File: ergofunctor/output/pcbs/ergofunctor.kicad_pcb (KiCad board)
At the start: 2 copper layers, 155.9 x 135.1 mm, 50 parts

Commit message: joystick adjustments for ergofunctor
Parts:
- removed TRRS1: TRRS-PJ-320A-dual, TRRS-PJ-320A-dual
- added H1: , ceoloide:mounting_hole_plated, F.Cu at (184.3, 144.1)
- added H2: , ceoloide:mounting_hole_plated, F.Cu at (162.6, 136.2)
- added XX1: , AMPHENOL_SFV5R-4STE1HLF, F.Cu at (179.9, 122.3)
- moved _2 10.0 mm to (173.9, 86.9)
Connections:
- _2 pad 1: pos -> B-
- _2 pad 2: B- -> pos
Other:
- board size 155.9 x 135.1 mm -> 161.5 x 130.8 mm

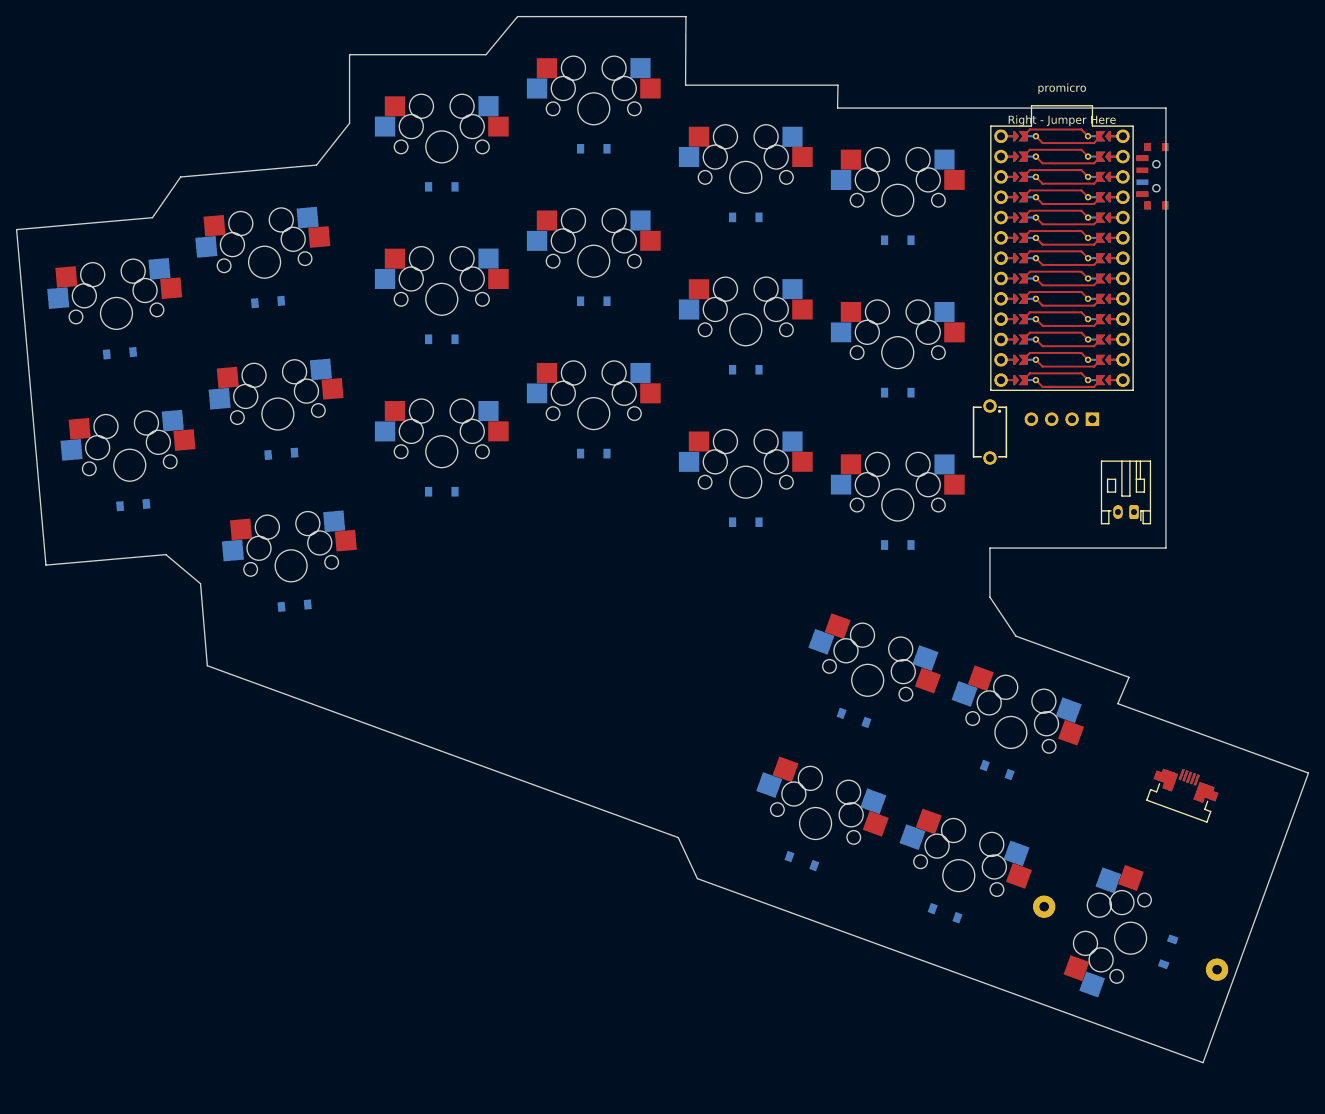
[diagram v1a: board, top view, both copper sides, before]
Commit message: change joystick and finish config
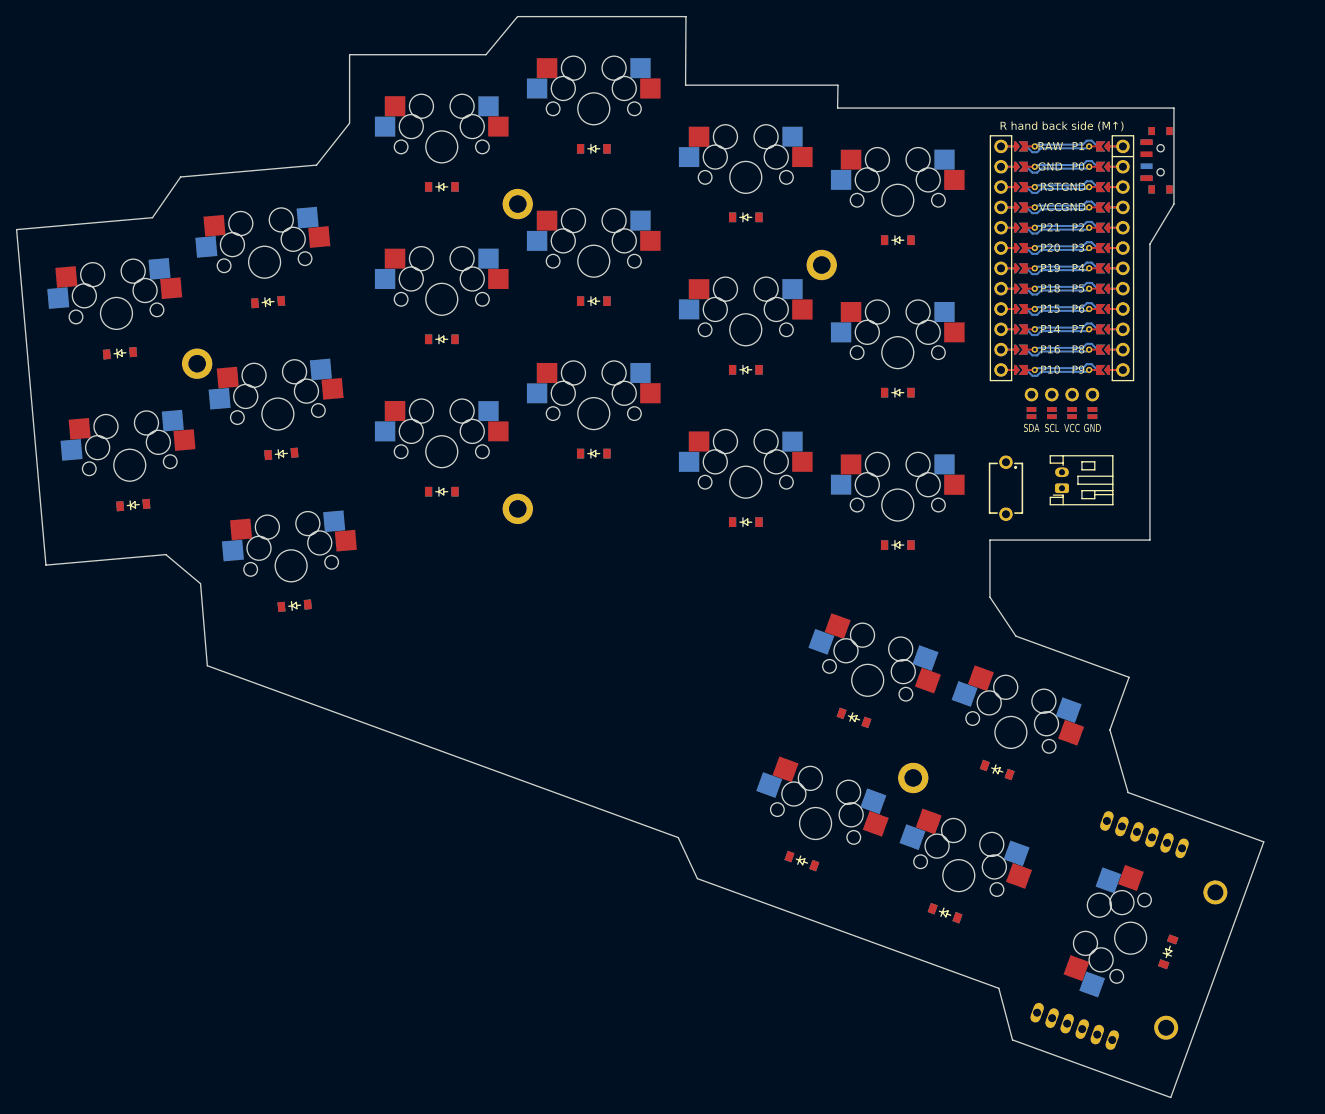
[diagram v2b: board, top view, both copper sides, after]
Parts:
- removed ?: , ProMicro
- removed OLED1: OLED, lib:OLED_headers
- removed _2: , Connector_JST:JST_PH_S2B-PH-K_1x02_P2.00mm_Horizontal
- added DISP1: , nice!view, F.Cu at (164.9, 88.9)
- added H3: , ceoloide:mounting_hole_plated, F.Cu at (96.8, 48.4)
- added H4: , ceoloide:mounting_hole_plated, F.Cu at (96.8, 86.5)
- added H5: , ceoloide:mounting_hole_plated, F.Cu at (146.3, 120.1)
- added MCU1: , ceoloide:mcu_supermini_nrf52840, F.Cu at (164.9, 53.9)
- added XX2: , joystick, F.Cu at (184.0, 134.4)
- added _1: , Connector_JST:JST_PH_S2B-PH-K_1x02_P2.00mm_Horizontal,  at (164.9, 83.9)
- D1, D10, D11, D12, D13, D14, D15, D16, D17, D18, D19, D2, D20, D21, D22, D3, D4, D5, D6, D7, D8, D9: moved to F.Cu
- XX1: footprint AMPHENOL_SFV5R-4STE1HLF -> joystick
- moved H1 148.3 mm to (56.8, 68.3), turned to 5 degrees
- moved H2 84.9 mm to (134.8, 56.0), turned to 0 degrees
- moved XX1 29.1 mm to (177.9, 151.3), turned to 70 degrees
- moved S23 7.30 mm to (157.9, 83.9)
- moved T1 2.07 mm to (176.9, 42.9)
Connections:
- T1 pad 1: pos -> sw1
- T1 pad 2: B+ -> RAW
- XX1 pad 2: P20 -> GND
- XX1 pad 3: P19 -> P20
- XX1 pad 4: GND -> P19
- XX1 pad 5: P21 -> GND
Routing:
- net (no net): track 371.4 -> 337.7 mm
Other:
- board size 161.5 x 130.8 mm -> 155.9 x 135.1 mm

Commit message: fix mcu-switchs connection
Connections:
- D1 pad 1: R_HOME -> P14
- D10 pad 1: R_HOME -> P14
- D11 pad 1: R_TOP -> P15
- D12 pad 1: R_BOT -> P16
- D13 pad 1: R_HOME -> P14
- D14 pad 1: R_TOP -> P15
- D15 pad 1: R_BOT -> P16
- D16 pad 1: R_HOME -> P14
- D17 pad 1: R_TOP -> P15
- D18 pad 1: R_THUMB -> P10
- D19 pad 1: R_THUMB -> P10
- D2 pad 1: R_TOP -> P15
- D20 pad 1: R_THUMB -> P10
- D21 pad 1: R_THUMB -> P10
- D22 pad 1: R_THUMB -> P10
- D3 pad 1: R_BOT -> P16
- D4 pad 1: R_HOME -> P14
- D5 pad 1: R_TOP -> P15
- D6 pad 1: R_BOT -> P16
- D7 pad 1: R_HOME -> P14
- D8 pad 1: R_TOP -> P15
- D9 pad 1: R_BOT -> P16
- S1 pad 1: C_P_OUTER -> P4
- S10 pad 1: C_M_MIDDLE -> P7
- S11 pad 1: C_M_MIDDLE -> P7
- S12 pad 1: C_M_INDEX -> P8
- S13 pad 1: C_M_INDEX -> P8
- S14 pad 1: C_M_INDEX -> P8
- S15 pad 1: C_M_INNER -> P9
- S16 pad 1: C_M_INNER -> P9
- S17 pad 1: C_M_INNER -> P9
- S18 pad 1: C_P_INNER -> P4
- S19 pad 1: C_M_RING -> P5
- S2 pad 1: C_P_OUTER -> P4
- S20 pad 1: C_M_MIDDLE -> P6
- S21 pad 1: C_M_INDEX -> P7
- S22 pad 1: C_M_INNER -> P8
- S3 pad 1: C_P_INNER -> P5
- S4 pad 1: C_P_INNER -> P5
- S5 pad 1: C_P_INNER -> P5
- S6 pad 1: C_M_RING -> P6
- S7 pad 1: C_M_RING -> P6
- S8 pad 1: C_M_RING -> P6
- S9 pad 1: C_M_MIDDLE -> P7

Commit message: fix connected columns
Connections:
- D18 pad 2: outer_row -> outer_top_row
- D19 pad 2: middle_row -> middle_top_row
- D20 pad 2: outer_row -> outer_bottom_row
- D21 pad 2: middle_row -> middle_bottom_row
- D3 pad 2: inner_bottom -> innerp_bottom
- D4 pad 2: inner_home -> innerp_home
- D5 pad 2: inner_top -> innerp_top
- S18 pad 2: outer_row -> outer_top_row
- S19 pad 2: middle_row -> middle_top_row
- S20 pad 2: outer_row -> outer_bottom_row
- S21 pad 2: middle_row -> middle_bottom_row
- S3 pad 2: inner_bottom -> innerp_bottom
- S4 pad 2: inner_home -> innerp_home
- S5 pad 2: inner_top -> innerp_top

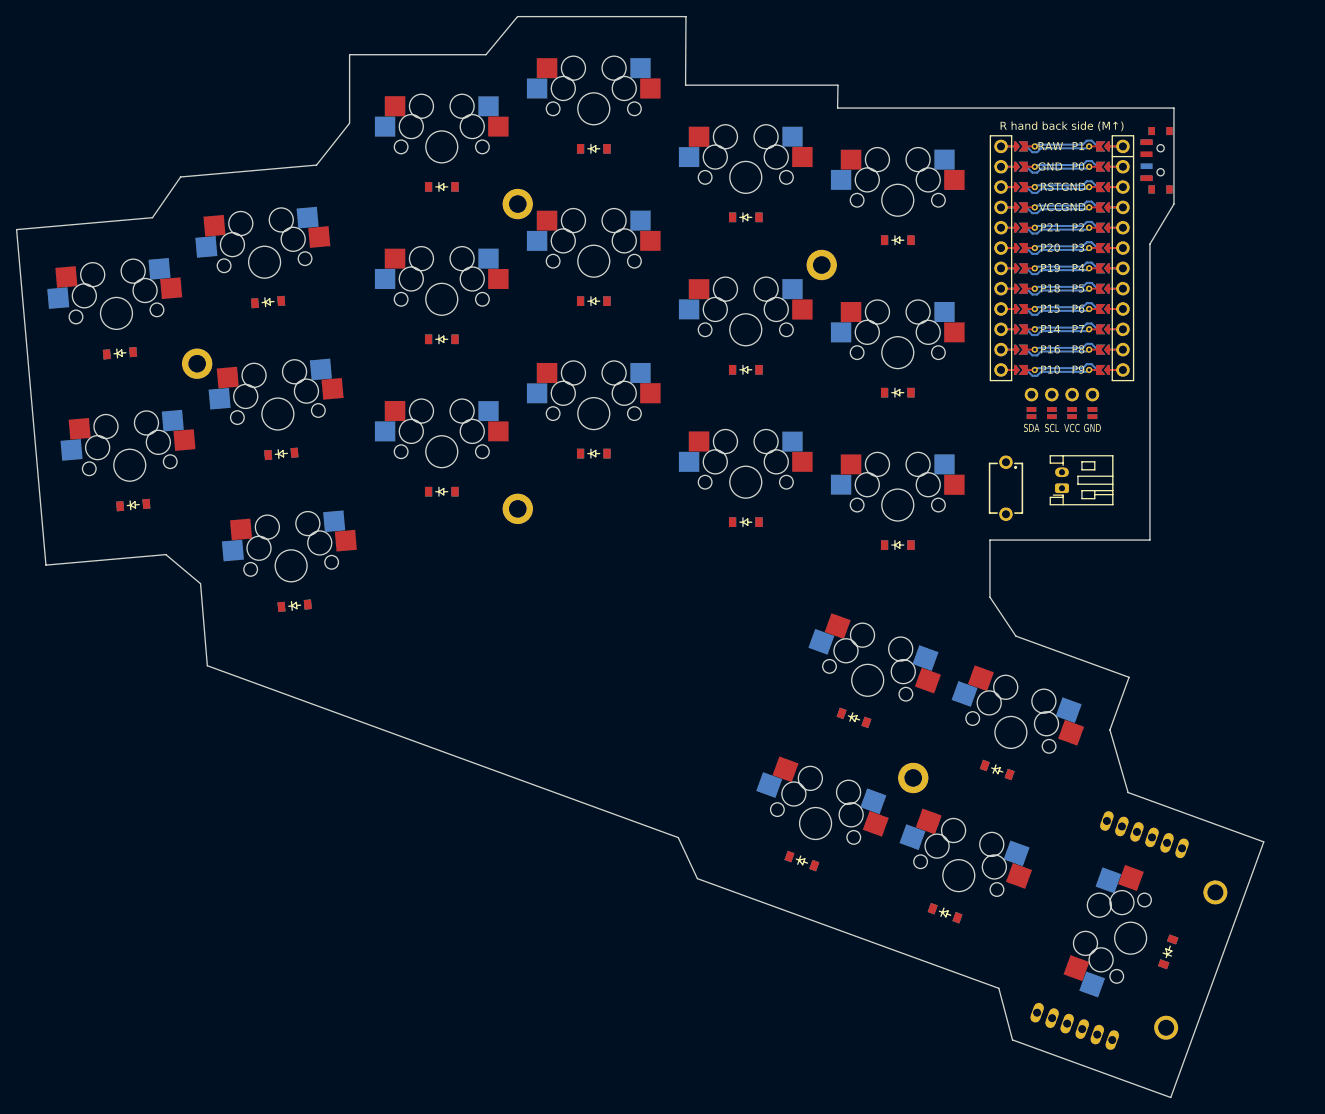
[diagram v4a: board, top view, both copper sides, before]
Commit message: add def kicad_pro to ergofunctor
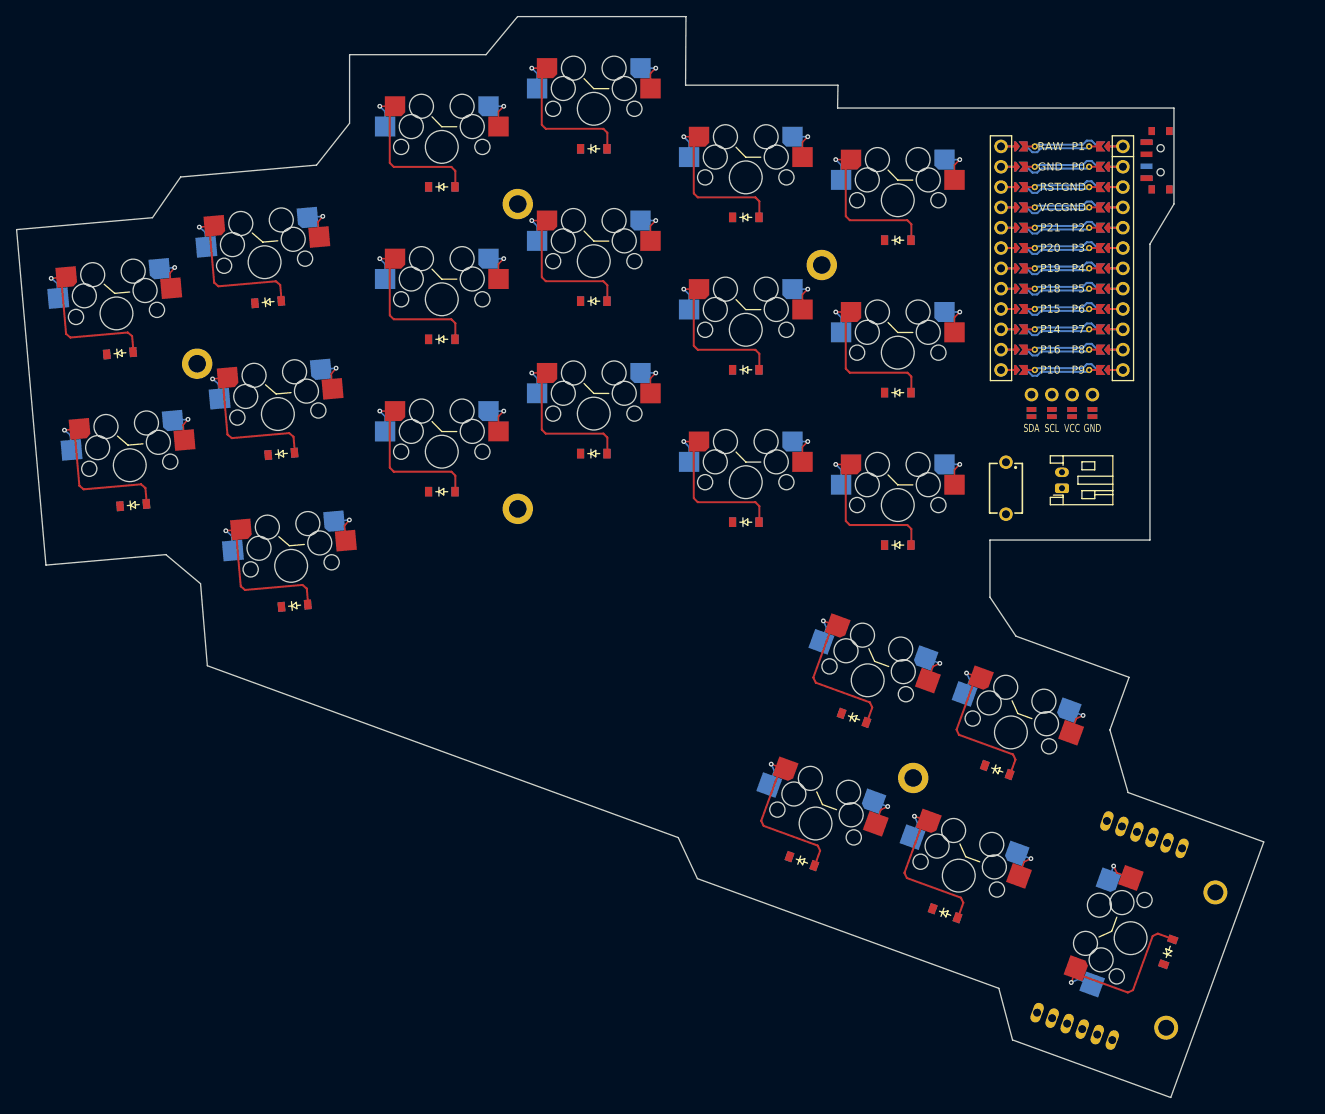
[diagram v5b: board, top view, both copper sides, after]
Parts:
- removed _1: , Connector_JST:JST_PH_S2B-PH-K_1x02_P2.00mm_Horizontal
- added _23: , Connector_JST:JST_PH_S2B-PH-K_1x02_P2.00mm_Horizontal,  at (164.9, 83.9)
- S1, S10, S11, S12, S13, S14, S15, S16, S17, S18, S19, S2, S20, S21, S22, S3, S4, S5, S6, S7, S8, S9: footprint MX -> ceoloide:switch_mx; moved to B.Cu
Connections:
- S1 pad 1: P4 -> outer_home
- S1 pad 2: outer_home -> P4
- S10 pad 1: P7 -> middle_home
- S10 pad 2: middle_home -> P7
- S11 pad 1: P7 -> middle_top
- S11 pad 2: middle_top -> P7
- S12 pad 1: P8 -> index_bottom
- S12 pad 2: index_bottom -> P8
- S13 pad 1: P8 -> index_home
- S13 pad 2: index_home -> P8
- S14 pad 1: P8 -> index_top
- S14 pad 2: index_top -> P8
- S15 pad 1: P9 -> inner_bottom
- S15 pad 2: inner_bottom -> P9
- S16 pad 1: P9 -> inner_home
- S16 pad 2: inner_home -> P9
- S17 pad 1: P9 -> inner_top
- S17 pad 2: inner_top -> P9
- S18 pad 1: P4 -> outer_top_row
- S18 pad 2: outer_top_row -> P4
- S19 pad 1: P5 -> middle_top_row
- S19 pad 2: middle_top_row -> P5
- S2 pad 1: P4 -> outer_top
- S2 pad 2: outer_top -> P4
- S20 pad 1: P6 -> outer_bottom_row
- S20 pad 2: outer_bottom_row -> P6
- S21 pad 1: P7 -> middle_bottom_row
- S21 pad 2: middle_bottom_row -> P7
- S22 pad 1: P8 -> inner_row
- S22 pad 2: inner_row -> P8
- S3 pad 1: P5 -> innerp_bottom
- S3 pad 2: innerp_bottom -> P5
- S4 pad 1: P5 -> innerp_home
- S4 pad 2: innerp_home -> P5
- S5 pad 1: P5 -> innerp_top
- S5 pad 2: innerp_top -> P5
- S6 pad 1: P6 -> ring_bottom
- S6 pad 2: ring_bottom -> P6
- S7 pad 1: P6 -> ring_home
- S7 pad 2: ring_home -> P6
- S8 pad 1: P6 -> ring_top
- S8 pad 2: ring_top -> P6
- S9 pad 1: P7 -> middle_bottom
- S9 pad 2: middle_bottom -> P7
- XX1 pad 4: P19 -> P8
- XX1 pad 5: GND -> inner_rowb
- XX2 pad 4: P19 -> P8
- XX2 pad 5: GND -> inner_rowb
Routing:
- net (no net): track 337.7 -> 731.1 mm
- net P7: track 0.00 -> 18.9 mm, vias 0 -> 4
- net P6: track 0.00 -> 18.9 mm, vias 0 -> 4
- net P8: track 0.00 -> 18.9 mm, vias 0 -> 4
- net P5: track 0.00 -> 18.9 mm, vias 0 -> 4
- net P9: track 0.00 -> 14.2 mm, vias 0 -> 3
- net P4: track 0.00 -> 14.2 mm, vias 0 -> 3
- net outer_top: track 0.00 -> 4.72 mm, vias 0 -> 1
- net innerp_top: track 0.00 -> 4.72 mm, vias 0 -> 1
- net outer_home: track 0.00 -> 4.72 mm, vias 0 -> 1
- net innerp_home: track 0.00 -> 4.72 mm, vias 0 -> 1
- net innerp_bottom: track 0.00 -> 4.72 mm, vias 0 -> 1
- net ring_top: track 0.00 -> 4.72 mm, vias 0 -> 1
- net ring_home: track 0.00 -> 4.72 mm, vias 0 -> 1
- net middle_top: track 0.00 -> 4.72 mm, vias 0 -> 1
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
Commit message: fix joystick
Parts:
- _23: moved to F.Cu
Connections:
- S1 pad 1: outer_home -> P4
- S10 pad 1: middle_home -> P7
- S11 pad 1: middle_top -> P7
- S12 pad 1: index_bottom -> P8
- S13 pad 1: index_home -> P8
- S14 pad 1: index_top -> P8
- S15 pad 1: inner_bottom -> P9
- S16 pad 1: inner_home -> P9
- S17 pad 1: inner_top -> P9
- S18 pad 1: outer_top_row -> P4
- S19 pad 1: middle_top_row -> P5
- S2 pad 1: outer_top -> P4
- S20 pad 1: outer_bottom_row -> P6
- S21 pad 1: middle_bottom_row -> P7
- S22 pad 1: inner_row -> P8
- S3 pad 1: innerp_bottom -> P5
- S4 pad 1: innerp_home -> P5
- S5 pad 1: innerp_top -> P5
- S6 pad 1: ring_bottom -> P6
- S7 pad 1: ring_home -> P6
- S8 pad 1: ring_top -> P6
- S9 pad 1: middle_bottom -> P7
- XX1 pad 5: inner_rowb -> inner_row
- XX2 pad 5: inner_rowb -> inner_row
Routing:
- net (no net): track 731.1 -> 0.00 mm
- net GND: track 0.00 -> 29.5 mm
- net middle_bottom_row: track 4.72 -> 22.6 mm
- net outer_top_row: track 4.72 -> 22.6 mm
- net inner_row: track 4.72 -> 22.6 mm
- net innerp_top: track 4.72 -> 22.6 mm
- net innerp_home: track 4.72 -> 22.6 mm
- net outer_home: track 4.72 -> 22.6 mm
- net outer_top: track 4.72 -> 22.6 mm
- net ring_bottom: track 4.72 -> 22.6 mm
- net index_bottom: track 4.72 -> 22.6 mm
- net middle_top: track 4.72 -> 22.6 mm
- net middle_bottom: track 4.72 -> 22.6 mm
- net ring_top: track 4.72 -> 22.6 mm
- net middle_home: track 4.72 -> 22.6 mm
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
